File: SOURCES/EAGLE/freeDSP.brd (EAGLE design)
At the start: 100 x 80 mm, 120 parts, among them IC1 24AA256P, IC3 AD8608R, Q1 12.288Mhz, Q2 2N7000, Q3 2N7000, Q4 2N7000, Q5 2N7000, T1 FZT751TA, X1 TOBU3, X2 TOBU3, X3 MKDSN1,5/2-5,08, X4 TOBU3, X5 TOBU3, X6 TOBU3, X7 TOBU3

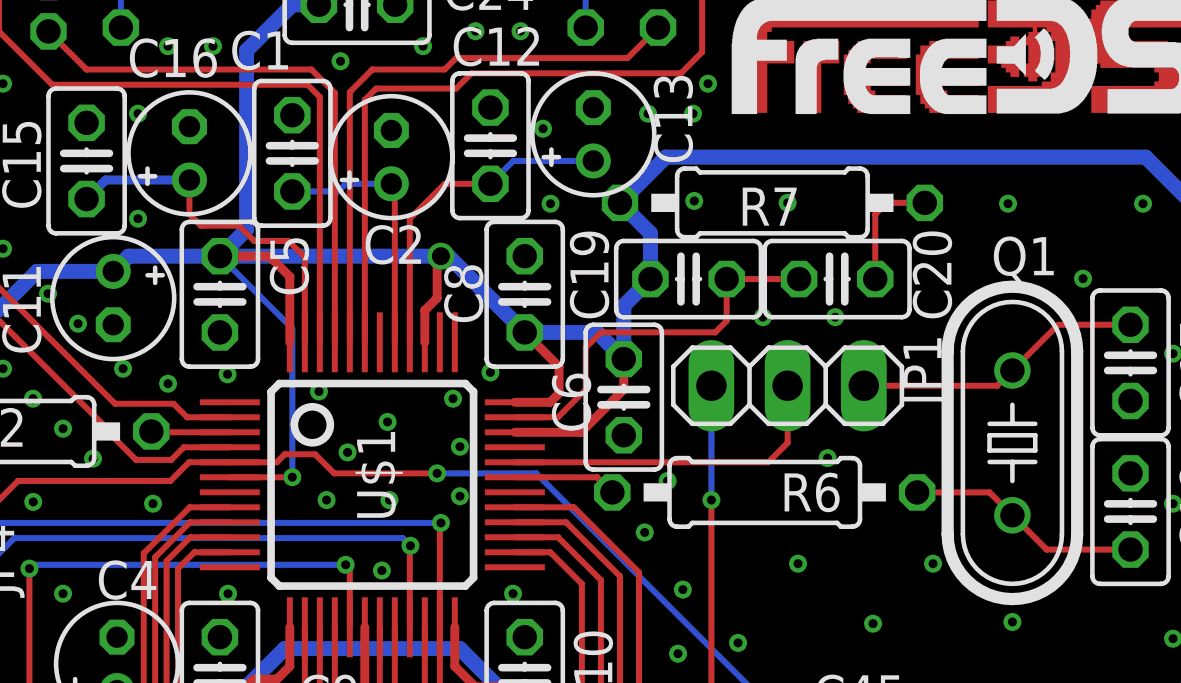
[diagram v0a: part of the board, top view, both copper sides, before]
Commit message: cleaned up the schematic and moved parts to different sheets
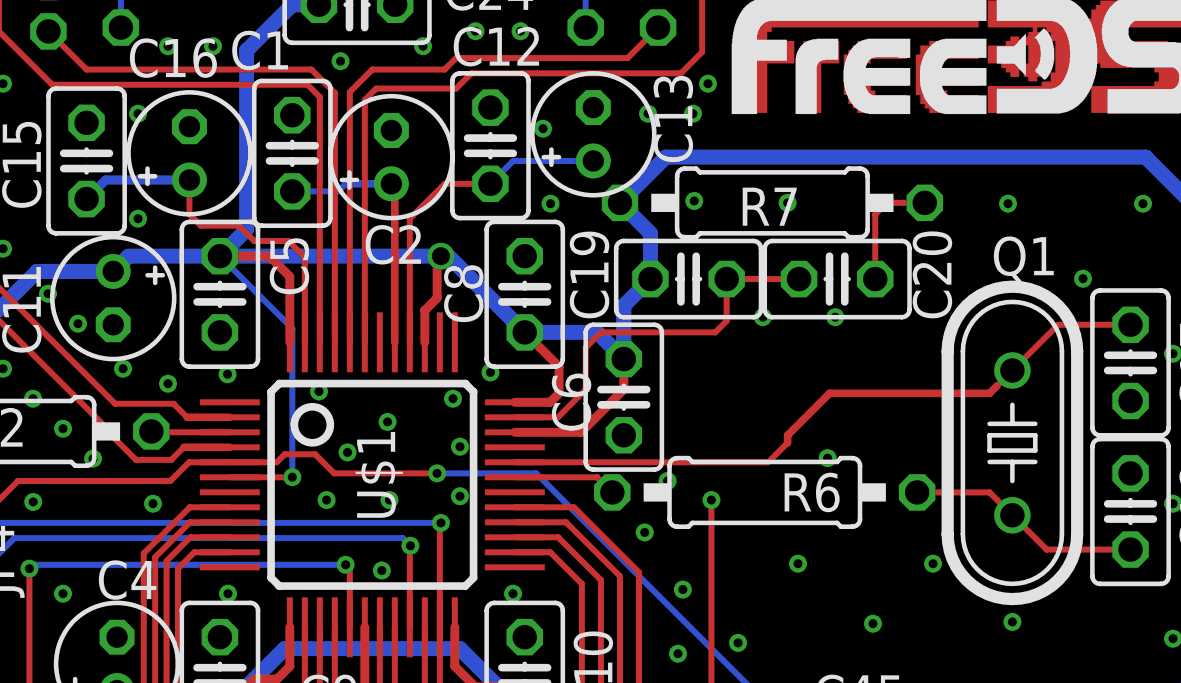
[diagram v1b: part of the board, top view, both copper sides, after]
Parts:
- removed JP1: (no value), pinhead:1X03
- R1: value 1k -> 1k 1%
- R2: value 18k -> 18k 1%
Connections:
- removed net N$40: R26.2, R30.2, R31.2, U$1.2
- removed net N$7: C17.2, JP1.1, Q1.1
- new net ADC1: R28.2, R32.2, R33.2, U$1.4
- net ADC0: now also R26.2, R30.2, R31.2, U$1.2; no longer R28.2, R32.2, R33.2, U$1.4
- net MCLK_IN: no longer JP1.3
- net N$10: now also C17.2, Q1.1; no longer JP1.2
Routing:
- net N$40: track 71.2 -> 0.00 mm
- net ADC1: track 0.00 -> 54.7 mm
- net ADC0: track 54.7 -> 71.2 mm
- net N$10: track 11.3 -> 22.6 mm
- net N$7: track 9.73 -> 0.00 mm
- net MCLK_IN: track 25.0 -> 21.2 mm

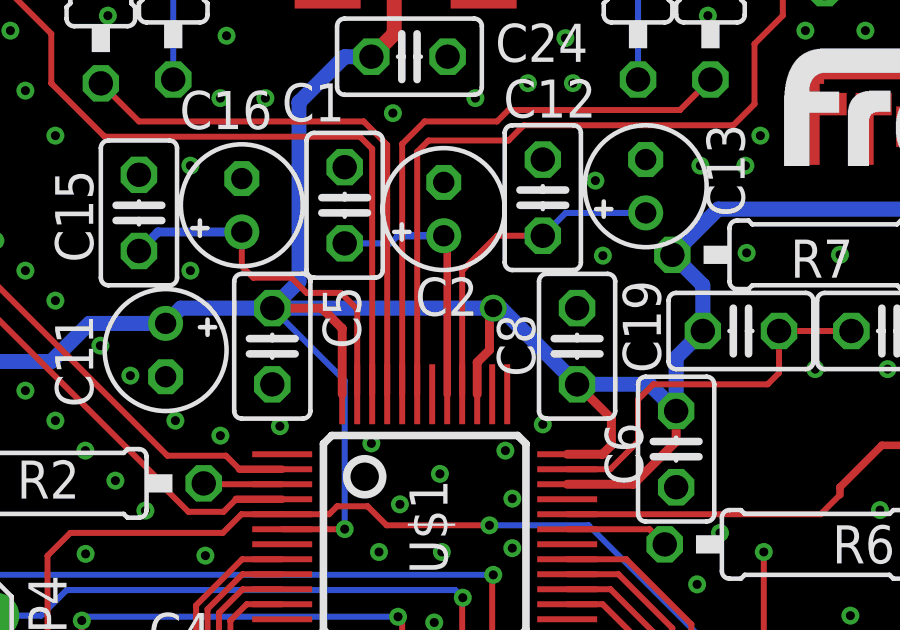
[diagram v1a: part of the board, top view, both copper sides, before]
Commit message: cleaned up sheet 0 and edited ADAU1701 to be smaller in the schematic
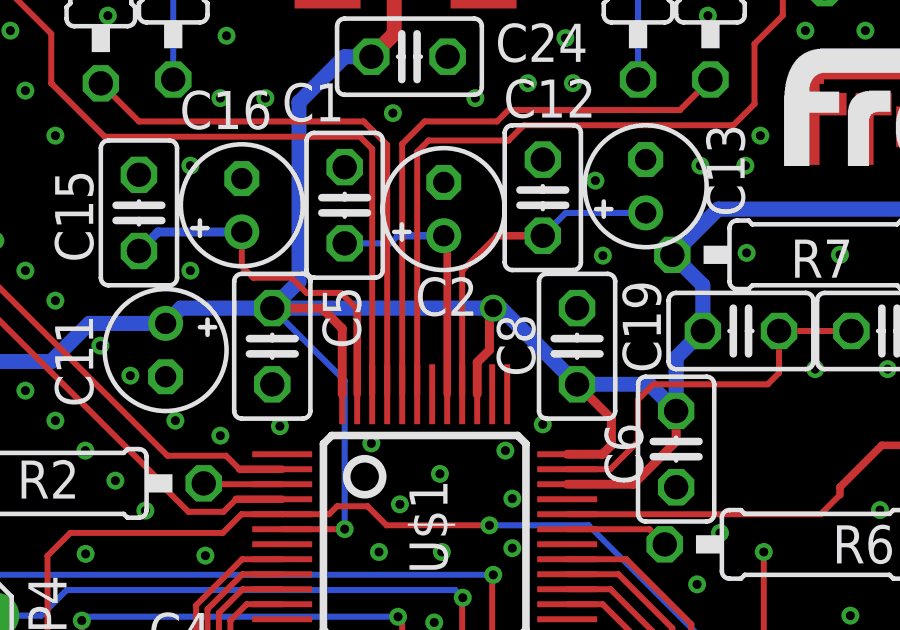
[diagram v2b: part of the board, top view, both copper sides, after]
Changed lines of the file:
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@@
 </signal>
 <signal name="FILTD">
+<contactref element="U$1" pad="41"/>
+<wire x1="68.06" y1="28.88" x2="68.06" y2="34.048" width="0.254" layer="1"/>
 <contactref element="C1" pad="1"/>
 <contactref element="C2" pad="+"/>
-<contactref element="U$1" pad="41"/>
 <wire x1="66.421" y1="34.163" x2="66.167" y2="33.909" width="0.2" layer="16"/>
 <wire x1="66.167" y1="33.909" x2="64.643" y2="33.909" width="0.2" layer="16"/>
 <wire x1="66.421" y1="34.163" x2="67.945" y2="34.163" width="0.254" layer="16"/>
-<wire x1="68.06" y1="28.88" x2="68.06" y2="34.048" width="0.254" layer="1"/>
 <wire x1="68.06" y1="34.048" x2="67.945" y2="34.163" width="0.254" layer="1"/>
 </signal>
@@
 </signal>
 <signal name="CM">
-<contactref element="C12" pad="1"/>
-<contactref element="C13" pad="+"/>
 <contactref element="U$1" pad="40"/>
 <wire x1="68.56" y1="28.88" x2="68.56" y2="33" width="0.2" layer="1"/>
 <wire x1="68.56" y1="33" x2="69.723" y2="34.163" width="0.2" layer="1"/>
-<wire x1="69.723" y1="34.163" x2="71.247" y2="34.163" width="0.2" layer="1"/>
+<contactref element="C12" pad="1"/>
+<contactref element="C13" pad="+"/>
 <wire x1="71.247" y1="34.163" x2="72.009" y2="34.925" width="0.2" layer="16"/>
 <wire x1="72.009" y1="34.925" x2="74.676" y2="34.925" width="0.2" layer="16"/>
+<wire x1="69.723" y1="34.163" x2="71.247" y2="34.163" width="0.254" layer="1"/>
 </signal>
 <signal name="FILTA">
 <contactref element="C16" pad="+"/>
 <contactref element="C15" pad="1"/>
-<contactref element="U$1" pad="47"/>
-<wire x1="65.06" y1="28.88" x2="65.06" y2="31.714" width="0.2" layer="1"/>
 <wire x1="65.06" y1="31.714" x2="64.516" y2="32.258" width="0.2" layer="1"/>
 <wire x1="64.516" y1="32.258" x2="63.373" y2="32.258" width="0.2" layer="1"/>
@@
 <wire x1="57.785" y1="33.655" x2="58.42" y2="34.29" width="0.3" layer="16"/>
 <wire x1="58.42" y1="34.29" x2="61.214" y2="34.29" width="0.3" layer="16"/>
+<contactref element="U$1" pad="47"/>
+<wire x1="65.06" y1="31.714" x2="65.06" y2="28.88" width="0.254" layer="1"/>
 </signal>
 <signal name="N$6">
